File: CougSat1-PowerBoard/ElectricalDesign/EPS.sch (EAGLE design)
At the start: 401 parts, among them J1 Deployable 0, J10 Battery -, J11 PGND, J12 Battery +, J13 VBatt, J2 PV0, J3 PV1, J4 Umbilical, J5 CougSat Card, J6 SWD, J7 PV2, J8 PV3, J9 Deployable 1, Q1 CSD25402Q3A, Q10 CSD25402Q3A, Q11 DMN53D0LDW, Q12 CSD25402Q3A, Q13 DMN53D0LDW, Q14 CSD25402Q3A, Q15 DMN53D0LDW, Q16 CSD25402Q3A, Q17 CSD25402Q3A, Q18 CSD25402Q3A, Q19 DMN53D0LDW, Q2 DMN2008LFU, Q20 CSD25402Q3A, Q21 CSD25402Q3A, Q22 CSD25402Q3A, Q23 DMN53D0LDW, Q24 CSD25402Q3A, Q25 DMN53D0LDW, Q26 CSD25402Q3A, Q27 DMN53D0LDW, Q28 CSD25402Q3A, Q29 CSD25402Q3A, Q3 DMN2008LFU, Q30 CSD25402Q3A, Q31 DMN53D0LDW, Q32 CSD25402Q3A, Q33 DMN53D0LDW, Q34 CSD25402Q3A, Q35 CSD25402Q3A, Q36 DMN53D0LDW, Q37 CSD25402Q3A, Q38 CSD25402Q3A, Q39 DMN53D0LDW, Q4 CSD25402Q3A, Q40 CSD25402Q3A, Q41 CSD25402Q3A, Q42 DMN53D0LDW, Q43 CSD25402Q3A, Q5 DMN53D0LDW, Q6 DMN53D0LDW, Q7 CSD25402Q3A, Q8 CSD25402Q3A, Q9 CSD25402Q3A, SW1 ESE24MH1, U1 INA199C2, U10 INA199C2, U11 INA199C1, U12 AD7689, U13 INA199C2, U14 INA199C2, U15 TXS0102DQM, U16 TXS0102DQM, U17 AD8515, U18 BQ29700, U19 INA199C2, U2 AD7689, U20 TXS0102DQM, U21 TXS0102DQM, U22 STM32L476RGT, U23 AD7291, U24 INA199C2, U25 INA199C2, U26 BQ29700, U27 INA199C2, U28 INA199C2, U29 INA199C2, U3 AD8515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

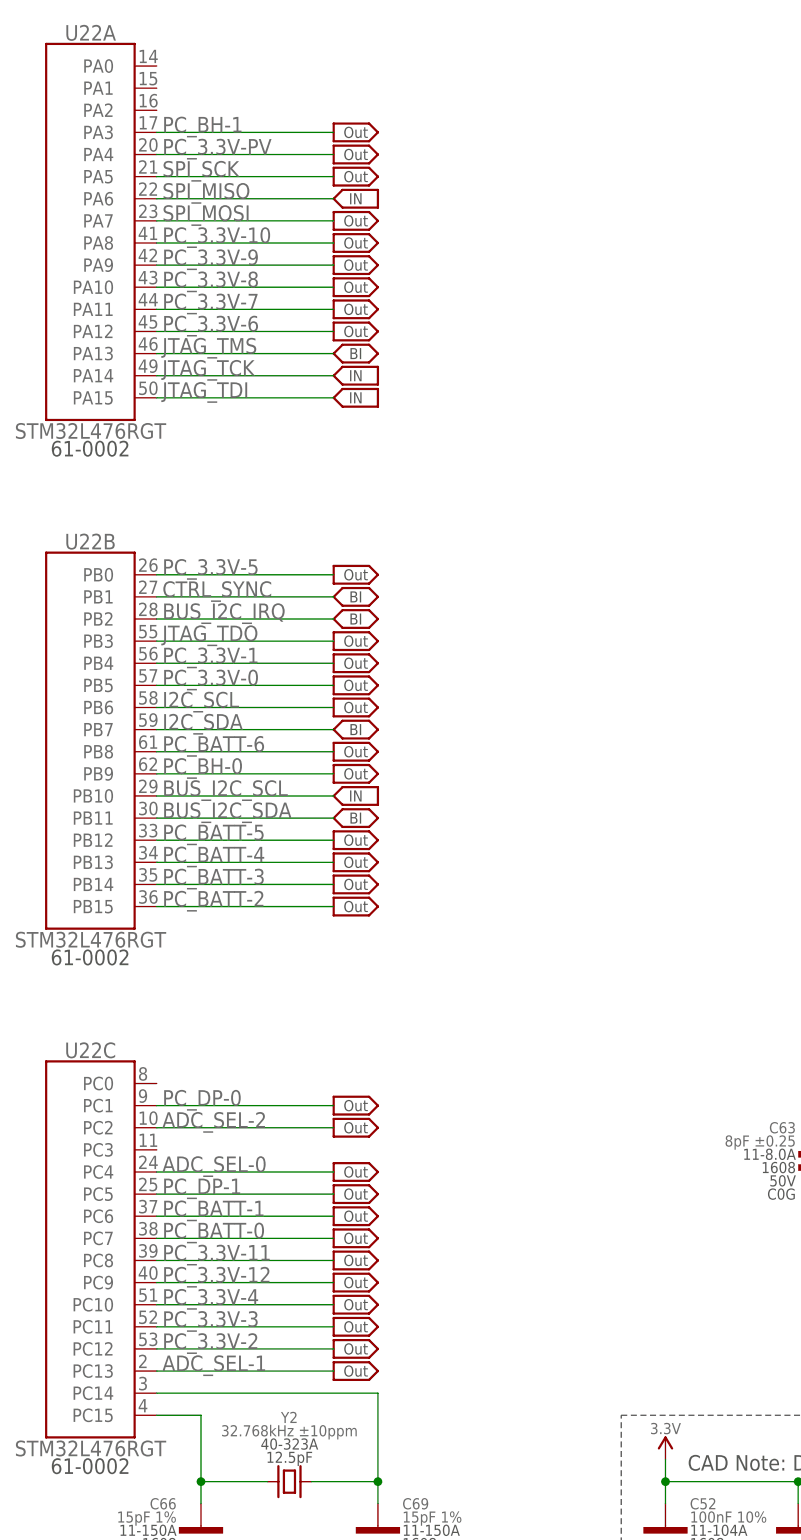
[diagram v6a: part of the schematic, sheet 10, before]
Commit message: Laid out µController
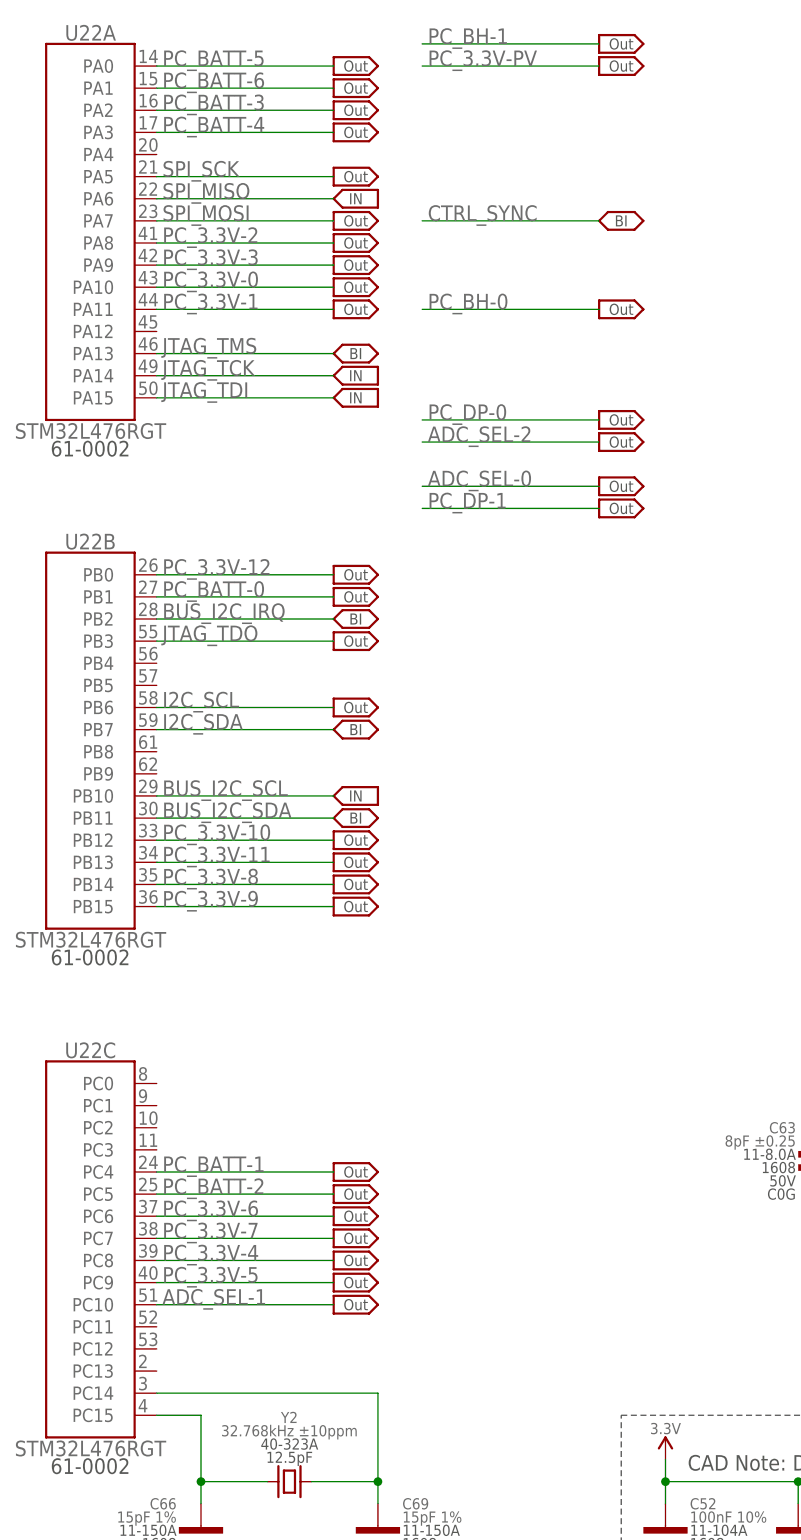
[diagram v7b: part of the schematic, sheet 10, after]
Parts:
- removed RN16: 5kΩ 0.1%, CougsInSpace-Resistors:RES-H-PAIRED-5K-1616
- added R36, R92: 0Ω <20mΩ, CougsInSpace-Resistors:RES-H-0-1608
- added RN4: 5kΩ 0.1%, CougsInSpace-Resistors:RES-H-PAIRED-5K-1616
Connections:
- removed net ADC_3.3V-A: RN16.A2, RN16.B2, U37.IN7
- new net ADC_3.3V-A1: RN4.A2, RN4.B2
- net 3.3V: now also RN4.B1; no longer RN16.B1
- net ADC_SEL-0: no longer U22C.PC4
- net ADC_SEL-1: now also U22C.PC10; no longer U22C.PC13
- net ADC_SEL-2: no longer U22C.PC2
- net ADC_VBATT-A: now also U37.IN7; no longer U12.IN0
- net AGND: now also RN4.A1, RT10.1; no longer C56.2, C58.2, RN16.A1, U23.AGND, U23.IN7
- net CHASSIS: now also R36.2, R92.2
- net CTRL_SYNC: no longer U22B.PB1
- net DEPLOY_SENSE-0: now also U37.IN6; no longer U12.IN2
- net I_3.3V_IN: no longer U37.IN5
- net I_3.3V_OUT: no longer U37.IN6
- net I_BATT_IN-A: now also U37.IN5; no longer U12.IN5
- net PC_3.3V-0: now also RN22.8, U22A.PA10; no longer RN22.1, U22B.PB5
- net PC_3.3V-1: now also RN22.1, U22A.PA11; no longer RN22.8, U22B.PB4
- net PC_3.3V-10: now also RN23.7, U22B.PB12; no longer RN23.2, U22A.PA8
- net PC_3.3V-11: now also RN23.2, U22B.PB13; no longer RN23.7, U22C.PC8
- net PC_3.3V-12: now also RN23.6, U22B.PB0; no longer RN23.3, U22C.PC9
- net PC_3.3V-2: now also RN22.7, U22A.PA8; no longer RN22.2, U22C.PC12
- net PC_3.3V-3: now also RN22.2, U22A.PA9; no longer RN22.7, U22C.PC11
- net PC_3.3V-4: now also RN22.6, U22C.PC8; no longer RN22.3, U22C.PC10
- net PC_3.3V-5: now also RN22.3, U22C.PC9; no longer RN22.6, U22B.PB0
- net PC_3.3V-6: now also RN22.5, U22C.PC6; no longer RN22.4, U22A.PA12
- net PC_3.3V-7: now also RN22.4, U22C.PC7; no longer RN22.5, U22A.PA11
- net PC_3.3V-8: now also RN23.8, U22B.PB14; no longer RN23.1, U22A.PA10
- net PC_3.3V-9: now also RN23.1, U22B.PB15; no longer RN23.8, U22A.PA9
- net PC_3.3V-PV: no longer U22A.PA4
- net PC_BATT-0: now also RN23.3, U22B.PB1; no longer RN23.6, U22C.PC7
- net PC_BATT-1: now also RN23.5, U22C.PC4; no longer RN23.4, U22C.PC6
- net PC_BATT-2: now also RN23.4, U22C.PC5; no longer RN23.5, U22B.PB15
- net PC_BATT-3: now also RN24.8, U22A.PA2; no longer RN24.1, U22B.PB14
- net PC_BATT-4: now also RN24.1, U22A.PA3; no longer RN24.8, U22B.PB13
- net PC_BATT-5: now also RN24.7, U22A.PA0; no longer RN24.2, U22B.PB12
- net PC_BATT-6: now also RN24.2, U22A.PA1; no longer RN24.7, U22B.PB8
- net PC_BH-0: no longer U22B.PB9
- net PC_BH-1: no longer U22A.PA3
- net PC_DP-0: no longer U22C.PC1
- net PC_DP-1: no longer U22C.PC5
- net PGND: now also C56.2, C58.2, R36.1, R92.1, U23.AGND, U23.IN7; no longer RT10.1
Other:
- moved on the sheet: RN15

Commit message: Laid out remaining traces
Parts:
- removed RT5, RT9: 10kΩ 5%, CougsInSpace-Resistors:THERMISTOR-V-10K-1608
- removed RT7: 10kΩ 5%, CougsInSpace-Resistors:THERMISTOR-H-10K-1608
- added TP17: TEST_POINT-SMD-C-1.25, CougsInSpace-Connectors:TEST_POINT-SMD-C-1.25
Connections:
- removed net ADC_3.3V-A1: RN4.A2, RN4.B2
- removed net TEMP-PCB-2: RN8.2, RT9.2, U5.IN2
- removed net TEMP-PCB-5: RN8.5, RT5.2, U5.IN7
- removed net TEMP-PMIC: RN8.6, RT7.2, U5.IN5
- new net ADC_3.3V: RN4.A2, RN4.B2, U2.IN4
- net !PC_DP-1: now also Q36B.D; no longer Q42A.D
- net ADC_EJECT_TIMER_BUF: now also U12.IN3; no longer U12.IN1
- net ADC_PV_IN-2A: now also U2.IN2; no longer U2.IN1
- net ADC_PV_IN-3A: now also U2.IN1; no longer U2.IN0
- net ADC_PV_IN-3B: now also U2.IN0; no longer U2.IN2
- net ADC_SEL-0: now also U22B.PB8
- net ADC_SEL-2: now also U22B.PB5
- net AGND: now also TP17.1, U2.IN7, U30.GND, U30.REF, U32.GND, U32.REF, U33.GND, U33.REF, U51.GND, U51.REF; no longer RT5.1, RT7.1, RT9.1, U2.IN4, U2.IN5, U2.IN6
- net CTRL_SYNC: now also U22A.PA4
- net DEPLOY_SENSE-1: now also U5.IN0; no longer U2.IN7
- net DGND: now also U12.IN0, U12.IN1, U12.IN2, U23.IN1, U23.IN6
- net I_3.3V-PV: now also U5.IN7; no longer U23.IN6
- net I_3.3V_IN: now also U2.IN6
- net I_3.3V_OUT: now also U2.IN5
- net I_BATT_IN-B: now also U12.IN4; no longer U12.IN3
- net I_BATT_OUT-B: now also U12.IN5; no longer U12.IN4
- net I_BH-0: now also U23.IN0
- net I_BH-1: now also U35.IN0
- net I_DP-0: now also U35.IN5; no longer U35.IN7
- net I_DP-1: now also U5.IN2; no longer U5.IN0
- net PC_3.3V-PV: now also U22B.PB4
- net PC_BATT-3: now also U22C.PC0; no longer U22A.PA2
- net PC_BATT-5: now also U22C.PC2; no longer U22A.PA0
- net PC_BATT-6: now also U22C.PC1; no longer U22A.PA1
- net PC_BH-0: now also RN24.6, U22A.PA2; no longer RN24.3
- net PC_BH-1: now also RN24.5, U22A.PA0; no longer RN24.6
- net PC_DP-0: now also U22A.PA1
- net PC_DP-1: now also Q36B.G, RN24.3, U22C.PC3; no longer Q42A.G, RN24.5
- net PGND: now also Q36B.S; no longer Q42A.S, U30.GND, U30.REF, U32.GND, U32.REF, U33.GND, U33.REF, U51.GND, U51.REF
- net TEMP-BATT-A: now also RN8.5, U5.IN5; no longer RN19.2, U35.IN5
- net TEMP-IN_SW-0: now also RN8.7, U5.IN3; no longer RN19.3, U35.IN3
- net TEMP-IN_SW-1: now also RN19.5, U35.IN7; no longer RN8.4, U5.IN6
- net TEMP-OUT_SW-0: now also RN19.1, U35.IN1; no longer RN19.5, U35.IN0
- net TEMP-OUT_SW-1: now also RN8.4, U5.IN6; no longer RN19.4, U35.IN1
- net TEMP-PCB-0: now also RN8.8; no longer RN8.1
- net TEMP-PCB-1: now also RN19.7, U35.IN4; no longer RN19.8, U35.IN6
- net TEMP-PCB-3: now also RN19.2, U35.IN3; no longer RN19.7, U35.IN4
- net TEMP-PCB-4: now also RN19.4, U35.IN6; no longer RN8.7, U5.IN3
- net TEMP-REG: now also RN19.8; no longer RN19.6
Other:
- moved on the sheet: RN10, RN4, RN6, RN7
